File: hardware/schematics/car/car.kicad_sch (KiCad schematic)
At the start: 21 parts, among them M1 Motor_Servo, M2 Motor_DC, Q1 Q_PMOS_Depletion, SW1 RotaryEncoder, SW2 SW_Push, SW3 SW_Push, U1 VL53L0CXV0DH1, U10 Mini-560, U2 VL53L0CXV0DH1, U3 VL53L0CXV0DH1, U4 Pixy2, U5 TXS0108EPW, U6 TB6612FNG, U7 SparkFun OTOS, U8 SWD debug probe, U9 Mini-360

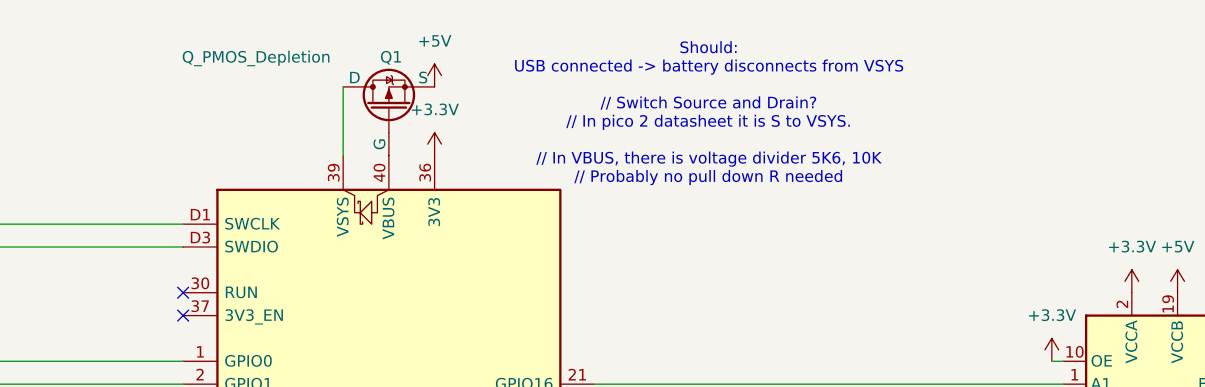
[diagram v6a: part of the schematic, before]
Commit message: [Schematic] mosfet fix. Use parasitic diode in our advantage
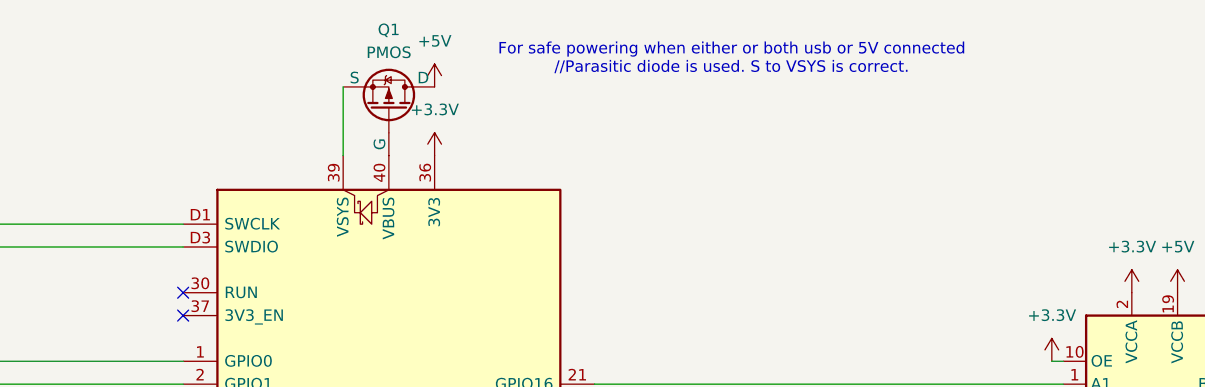
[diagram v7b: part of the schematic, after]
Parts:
- removed Q1: Q_PMOS_Depletion, Connector_PinHeader_2.54mm:PinHeader_1x03_P2.54mm_Vertical, symbol Device:Q_PMOS_Depletion
- added Q1: PMOS, Package_TO_SOT_THT:TO-247-3_Vertical, symbol Simulation_SPICE:PMOS
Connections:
- net +5V: now also Q1.1 (D)
- net at A1.39 (VSYS): now also Q1.3 (S)
- net at A1.40 (VBUS): now also Q1.2 (G)
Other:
- note added: "For safe powering when either or both usb or 5V connected //Parasitic diode is used. S to VSYS is correct."
- note removed: "Should: USB connected -> battery disconnects from VSYS // Switch Source and Drain? // In pico 2 datasheet it is S to VSYS. // In VBUS, there is voltage divider 5K6, 10K // Probably no pull down R needed"
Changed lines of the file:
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@@
 		)
 	)
-	(text "Should:\nUSB connected -> battery disconnects from VSYS\n\n// Switch Source and Drain?\n// In pico 2 datasheet it is S to VSYS.\n\n// In VBUS, there is voltage divider 5K6, 10K\n// Probably no pull down R needed"
+	(text "For safe powering when either or both usb or 5V connected\n//Parasitic diode is used. S to VSYS is correct."
 		(exclude_from_sim yes)
-		(at 176.53 24.638 0)
+		(at 179.07 18.542 0)
 		(effects
 			(font
@@
 	)
 	(symbol
-		(lib_id "Device:Q_PMOS_Depletion")
-		(at 140.97 24.13 90)
-		(unit 1)
-		(body_style 1)
-		(exclude_from_sim no)
-		(in_bom yes)
-		(on_board yes)
-		(in_pos_files yes)
-		(dnp no)
-		(property "Reference" "Q1"
-			(at 141.224 18.288 90)
-			(show_name no)
-			(do_not_autoplace no)
-			(effects
-				(font
-					(size 1.27 1.27)
-				)
-			)
-		)
-		(property "Value" "Q_PMOS_Depletion"
-			(at 126.238 18.288 90)
-			(show_name no)
-			(do_not_autoplace no)
-			(effects
-				(font
-					(size 1.27 1.27)
-				)
-			)
-		)
-		(property "Footprint" "Connector_PinHeader_2.54mm:PinHeader_1x03_P2.54mm_Vertical"
-			(at 138.43 19.05 0)
-			(hide yes)
-			(show_name no)
-			(do_not_autoplace no)
-			(effects
-				(font
-					(size 1.27 1.27)
-				)
-			)
-		)
-		(property "Datasheet" ""
-			(at 140.97 24.13 0)
-			(hide yes)
-			(show_name no)
-			(do_not_autoplace no)
-			(effects
-				(font
-					(size 1.27 1.27)
-				)
-			)
-		)
-		(property "Description" "Depletion-mode P-channel MOSFET"
-			(at 140.97 24.13 0)
-			(hide yes)
-			(show_name no)
-			(do_not_autoplace no)
-			(effects
-				(font
-					(size 1.27 1.27)
-				)
-			)
-		)
-		(pin "G"
-		)
-		(pin "S"
-		)
-		(pin "D"
-		)
-		(instances
-			(project "car"
-				(path "/5e1ba60a-5dff-4ce7-a8b0-cf19f27fe16e"
-					(reference "Q1")
-					(unit 1)
-				)
-			)
-		)
-	)
-	(symbol
 		(lib_id "power:+12V")
 		(at 229.87 138.43 90)
@@
 					(unit 1)
 				)
+			)
+		)
+	)
+	(symbol
+		(lib_id "Simulation_SPICE:PMOS")
+		(at 140.97 24.13 270)
+		(mirror x)
+		(unit 1)
+		(body_style 1)
+		(exclude_from_sim no)
+		(in_bom yes)
+		(on_board yes)
+		(in_pos_files yes)
+		(dnp no)
+		(fields_autoplaced yes)
+		(property "Reference" "Q1"
+			(at 140.97 15.24 90)
+			(show_name no)
+			(do_not_autoplace no)
+			(effects
+				(font
+					(size 1.27 1.27)
+				)
+			)
+		)
+		(property "Value" "PMOS"
+			(at 140.97 17.78 90)
+			(show_name no)
+			(do_not_autoplace no)
+			(effects
+				(font
+					(size 1.27 1.27)
+				)
+			)
+		)
+		(property "Footprint" "Package_TO_SOT_THT:TO-247-3_Vertical"
+			(at 143.51 19.05 0)
+			(hide yes)
+			(show_name no)
+			(do_not_autoplace no)
+			(effects
+				(font
+					(size 1.27 1.27)
+				)
+			)
+		)
+		(property "Datasheet" "https://ngspice.sourceforge.io/docs/ngspice-html-manual/manual.xhtml#cha_MOSFETs"
+			(at 128.27 24.13 0)
+			(hide yes)
+			(show_name no)
+			(do_not_autoplace no)
+			(effects
+				(font
+					(size 1.27 1.27)
+				)
+			)
+		)
+		(property "Description" "P-MOSFET transistor, drain/source/gate"
+			(at 140.97 24.13 0)
+			(hide yes)
+			(show_name no)
+			(do_not_autoplace no)
+			(effects
+				(font
+					(size 1.27 1.27)
+				)
+			)
+		)
+		(property "Sim.Device" "PMOS"
+			(at 123.825 24.13 0)
+			(hide yes)
+			(show_name no)
+			(do_not_autoplace no)
+			(effects
+				(font
+					(size 1.27 1.27)
+				)
+			)
+		)
+		(property "Sim.Type" "VDMOS"
+			(at 121.92 24.13 0)
+			(hide yes)
+			(show_name no)
+			(do_not_autoplace no)
+			(effects
+				(font
+					(size 1.27 1.27)
+				)
+			)
+		)
+		(property "Sim.Pins" "1=D 2=G 3=S"
+			(at 125.73 24.13 0)
+			(hide yes)
+			(show_name no)
+			(do_not_autoplace no)
+			(effects
+				(font
+					(size 1.27 1.27)
+				)
+			)
+		)
+		(pin "3"
+		)
+		(pin "2"
+		)
+		(pin "1"
+		)
+		(instances
+			(project "car"
+				(path "/5e1ba60a-5dff-4ce7-a8b0-cf19f27fe16e"
+					(reference "Q1")
+					(unit 1)
+				)

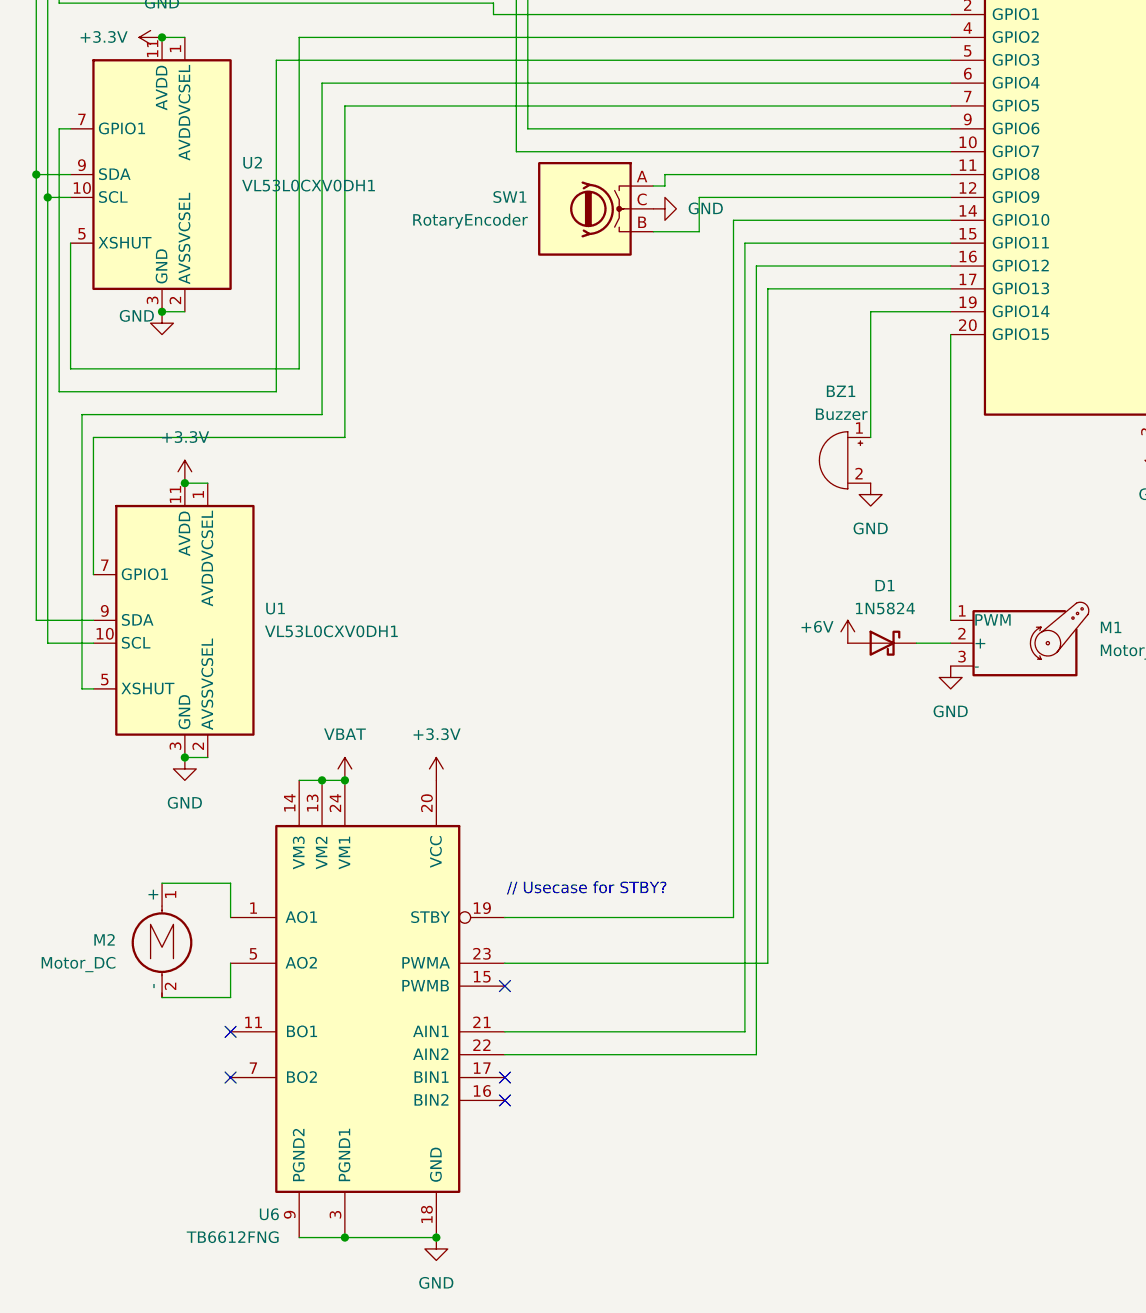
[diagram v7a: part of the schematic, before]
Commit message: [Schematic] use jga motor connector instead
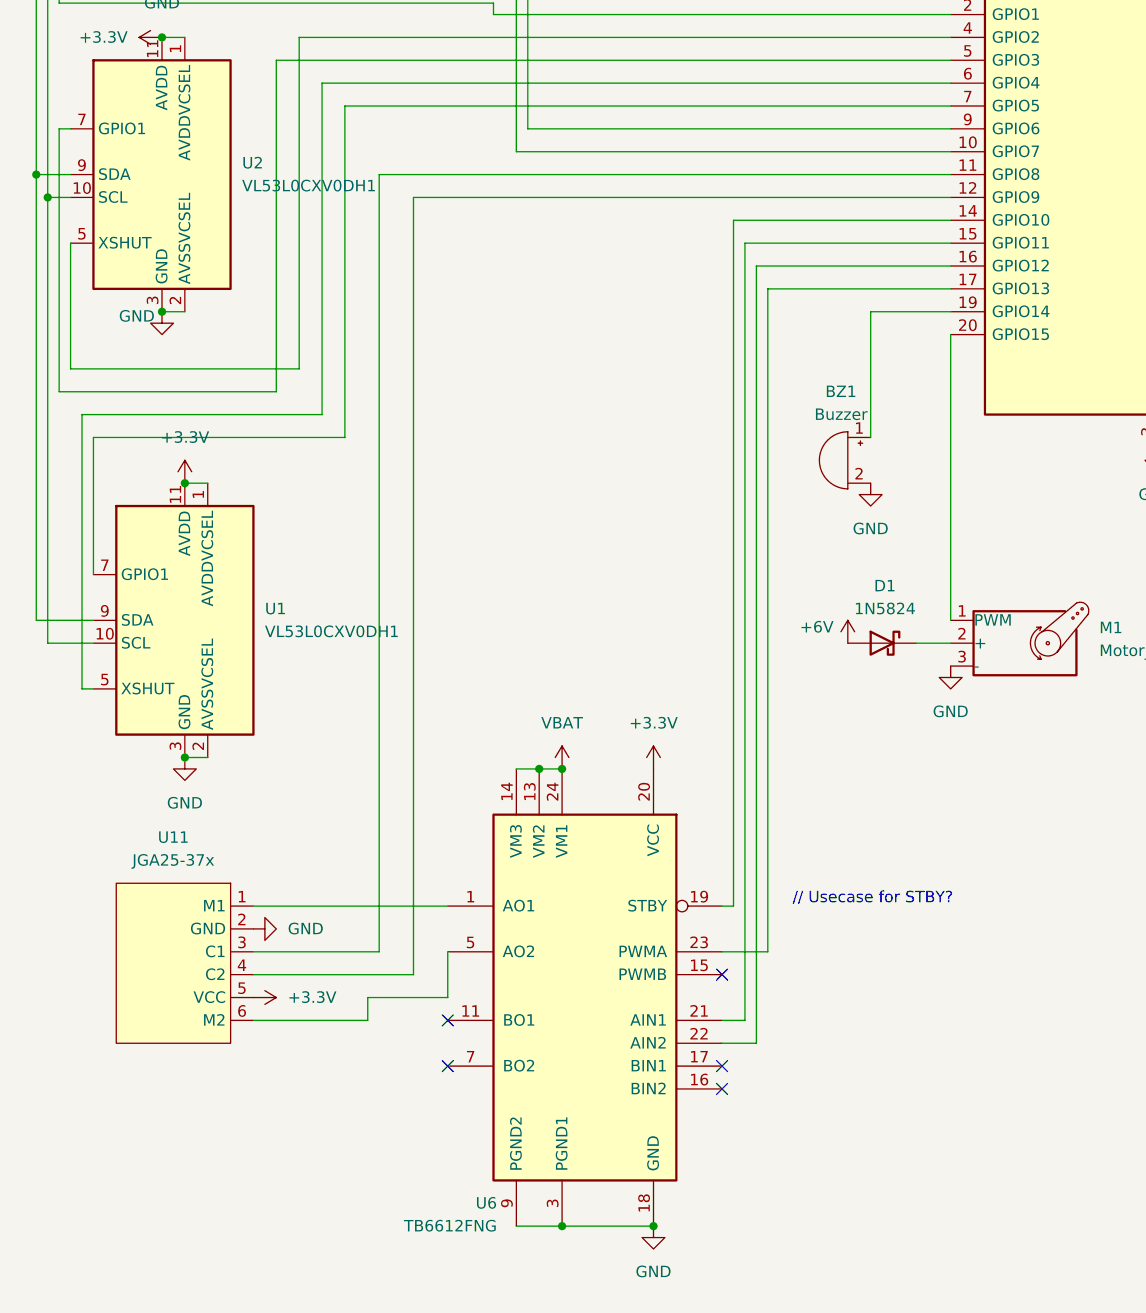
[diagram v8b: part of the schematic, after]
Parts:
- removed M2: Motor_DC, symbol Motor:Motor_DC
- removed SW1: RotaryEncoder, Connector_PinHeader_2.54mm:PinHeader_1x02_P2.54mm_Vertical, symbol Device:RotaryEncoder
- added U11: JGA25-37x, Connector_PinHeader_2.54mm:PinHeader_1x06_P2.54mm_Vertical, symbol xlnc_apex:JGA25-37x
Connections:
- net +3.3V: now also U11.5 (VCC)
- net GND: now also U11.2 (GND)
- net at U6.1 (AO1), U6.2 (AO1): now also U11.1 (M1)
- net at U6.5 (AO2), U6.6 (AO2): now also U11.6 (M2)
- net at A1.11 (GPIO8): now also U11.3 (C1)
- net at A1.12 (GPIO9): now also U11.4 (C2)
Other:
- moved on the sheet: U6
